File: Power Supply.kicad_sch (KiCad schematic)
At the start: 12 parts

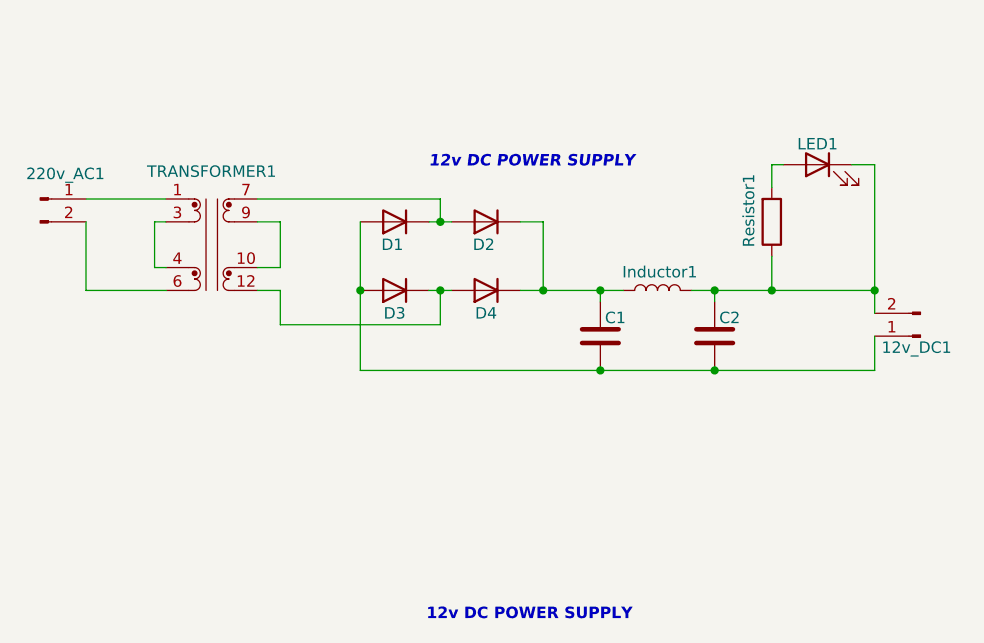
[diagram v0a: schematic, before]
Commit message: Added Copper fill in back-layer
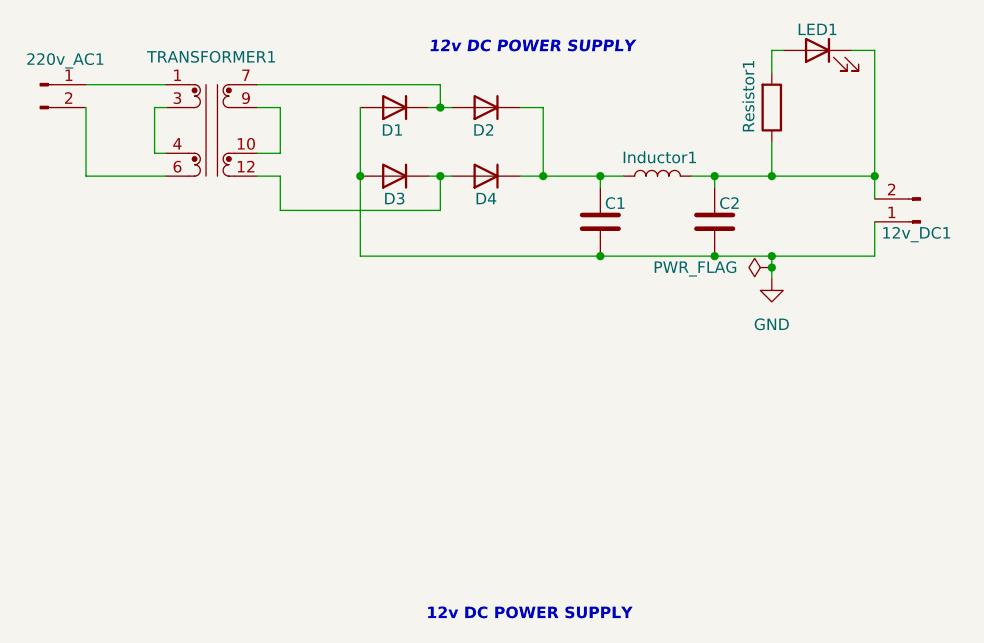
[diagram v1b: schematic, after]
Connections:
- net GND: now reaches 12v_DC1.1 (Pin_1), C1.2, C2.2, D1.2 (A), D3.2 (A)
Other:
- moved on the sheet: 12v_DC1, 220v_AC1, C1, C2, D1, D2, D3, D4, Inductor1, LED1, Resistor1, TRANSFORMER1
